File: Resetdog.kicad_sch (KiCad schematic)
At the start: 19 parts, among them U14 MC14541BD, U15 MC74HC4538ADG, U20 74LVC1G17

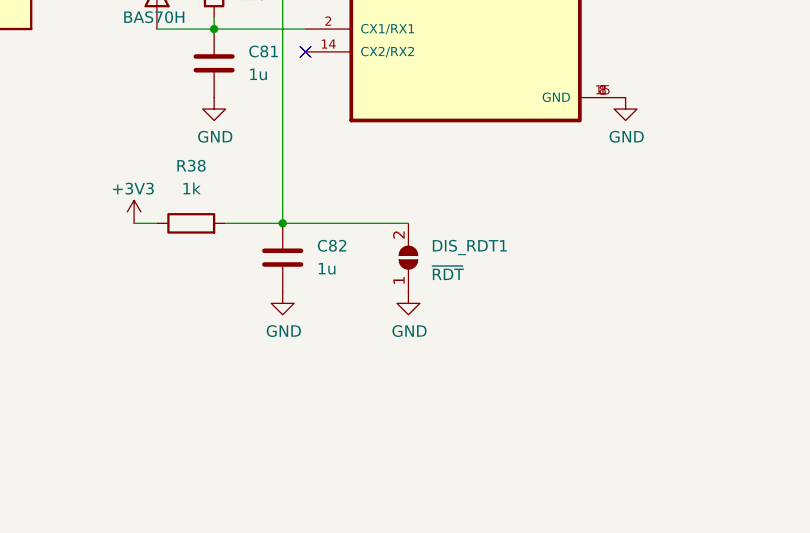
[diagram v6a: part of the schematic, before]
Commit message: Remove disable RTD jumper
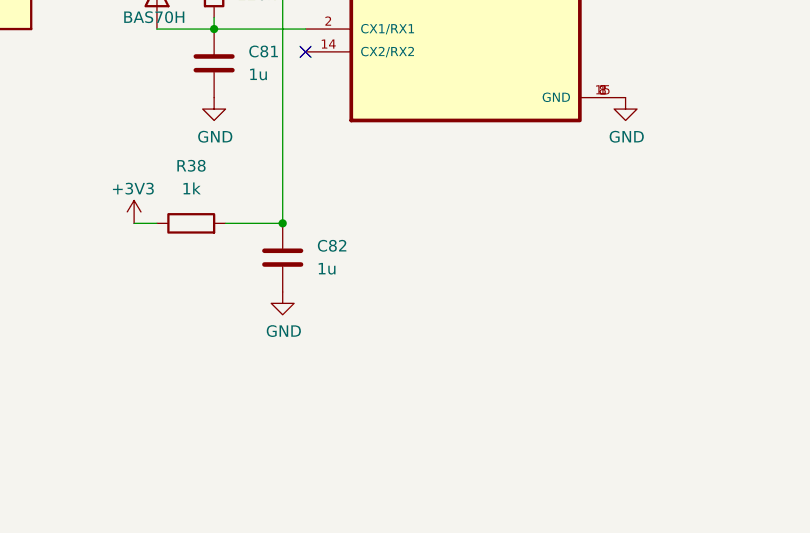
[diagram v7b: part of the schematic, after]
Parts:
- removed DIS_RDT1: ~{RDT}, Jumper:SolderJumper-2_P1.3mm_Open_Pad1.0x1.5mm, symbol Jumper:SolderJumper_2_Open
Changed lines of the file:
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@@
-    (stroke (width 0) (type default) (color 0 0 0 0))
-  )
-  (wire (pts (xy 134.62 119.38) (xy 148.59 119.38))
     (stroke (width 0) (type default) (color 0 0 0 0))
   )
@@
     (pin "2")
   )
-  (symbol (lib_id "power:GND") (at 148.59 127 0) (unit 1)
-    (in_bom yes) (on_board yes)
-    (property "Reference" "#PWR077" (id 0) (at 148.59 133.35 0)
-      (effects (font (size 1.27 1.27)) hide)
-    )
-    (property "Value" "GND" (id 1) (at 148.717 131.3942 0))
-    (property "Footprint" "" (id 2) (at 148.59 127 0)
-      (effects (font (size 1.27 1.27)) hide)
-    )
-    (property "Datasheet" "" (id 3) (at 148.59 127 0)
-      (effects (font (size 1.27 1.27)) hide)
-    )
-    (pin "1")
-  )
   (symbol (lib_id "Device:D") (at 120.65 93.98 270) (unit 1)
     (in_bom yes) (on_board yes)
@@
     (pin "1")
   )
-  (symbol (lib_id "Jumper:SolderJumper_2_Open") (at 148.59 123.19 90) (unit 1)
-    (in_bom no) (on_board yes) (fields_autoplaced)
-    (property "Reference" "DIS_RDT1" (id 0) (at 151.13 121.9199 90)
-      (effects (font (size 1.27 1.27)) (justify right))
-    )
-    (property "Value" "~{RDT}" (id 1) (at 151.13 125.0949 90)
-      (effects (font (size 1.27 1.27)) (justify right))
-    )
-    (property "Footprint" "Jumper:SolderJumper-2_P1.3mm_Open_Pad1.0x1.5mm" (id 2) (at 148.59 123.19 0)
-      (effects (font (size 1.27 1.27)) hide)
-    )
-    (property "Datasheet" "~" (id 3) (at 148.59 123.19 0)
-      (effects (font (size 1.27 1.27)) hide)
-    )
-    (pin "1")
-    (pin "2")
-  )
   (symbol (lib_id "power:+3V3") (at 40.64 127 0) (mirror y) (unit 1)

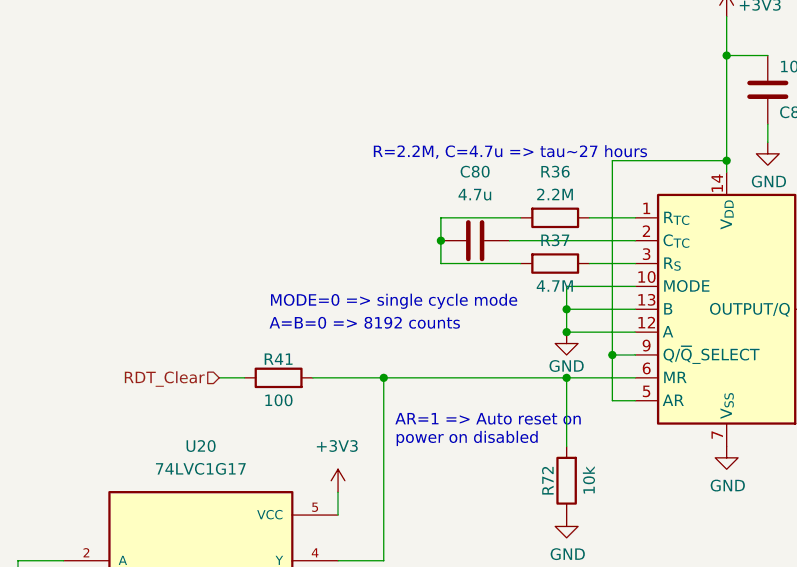
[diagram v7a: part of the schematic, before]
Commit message: Switch RTD MC14541BD IC from single cycle mode to recycle mode, but leave an option to switch back
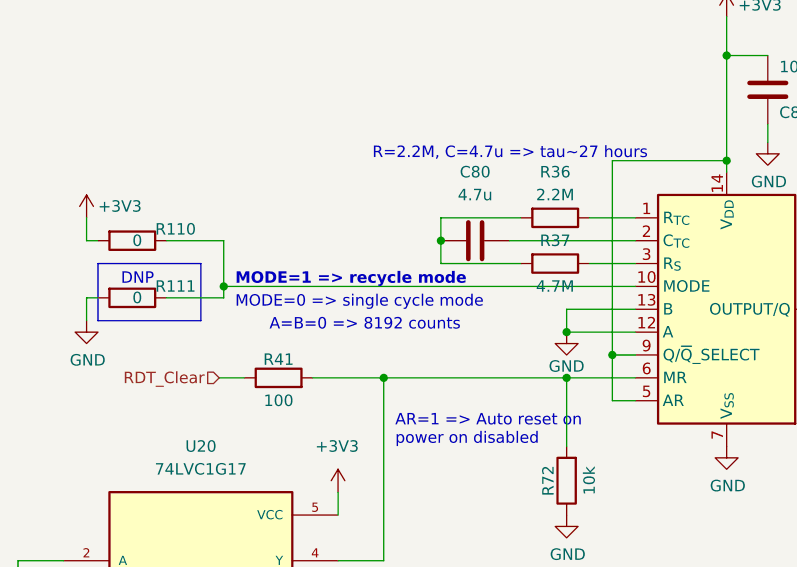
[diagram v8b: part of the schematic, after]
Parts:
- added R110, R111: 0, Resistor_SMD:R_0603_1608Metric, symbol Device:R
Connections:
- net +3V3: now also R110.2
- net GND: now also R111.2; no longer U14.10 (MODE)
- new net: R110.1, R111.1, U14.10 (MODE)
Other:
- note added: "DNP"
- note added: "MODE=1 => recycle mode"
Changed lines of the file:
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@@
   (junction (at 99.06 68.58) (diameter 0) (color 0 0 0 0)
   )
-  (junction (at 81.28 85.09) (diameter 0) (color 0 0 0 0)
-  )
   (junction (at 40.64 137.16) (diameter 0) (color 0 0 0 0)
   )
   (junction (at 99.06 56.896) (diameter 0) (color 0 0 0 0)
+  )
+  (junction (at 43.18 82.55) (diameter 0) (color 0 0 0 0)
   )
   (junction (at 67.31 77.47) (diameter 0) (color 0 0 0 0)
@@
     (stroke (width 0) (type default) (color 0 0 0 0))
   )
+  (polyline (pts (xy 29.21 80.01) (xy 29.21 86.36))
+    (stroke (width 0) (type default) (color 0 0 0 0))
+  )
+  (wire (pts (xy 43.18 77.47) (xy 43.18 82.55))
+    (stroke (width 0) (type default) (color 0 0 0 0))
+  )
   (wire (pts (xy 81.28 92.71) (xy 81.28 100.33))
     (stroke (width 0) (type default) (color 0 0 0 0))
   )
+  (wire (pts (xy 27.94 77.47) (xy 27.94 74.93))
+    (stroke (width 0) (type default) (color 0 0 0 0))
+  )
   (wire (pts (xy 180.34 85.09) (xy 180.34 67.31))
     (stroke (width 0) (type default) (color 0 0 0 0))
@@
     (stroke (width 0) (type default) (color 0 0 0 0))
   )
+  (polyline (pts (xy 29.21 86.36) (xy 40.64 86.36))
+    (stroke (width 0) (type default) (color 0 0 0 0))
+  )
   (wire (pts (xy 88.9 85.09) (xy 81.28 85.09))
     (stroke (width 0) (type default) (color 0 0 0 0))
@@
     (stroke (width 0) (type default) (color 0 0 0 0))
   )
+  (wire (pts (xy 43.18 82.55) (xy 88.9 82.55))
+    (stroke (width 0) (type default) (color 0 0 0 0))
+  )
+  (polyline (pts (xy 29.21 80.01) (xy 40.64 80.01))
+    (stroke (width 0) (type default) (color 0 0 0 0))
+  )
   (wire (pts (xy 83.82 74.93) (xy 88.9 74.93))
     (stroke (width 0) (type default) (color 0 0 0 0))
@@
     (stroke (width 0) (type default) (color 0 0 0 0))
   )
+  (polyline (pts (xy 40.64 86.36) (xy 40.64 80.01))
+    (stroke (width 0) (type default) (color 0 0 0 0))
+  )
   (wire (pts (xy 81.28 87.63) (xy 88.9 87.63))
     (stroke (width 0) (type default) (color 0 0 0 0))
   )
+  (wire (pts (xy 29.21 83.82) (xy 27.94 83.82))
+    (stroke (width 0) (type default) (color 0 0 0 0))
+  )
   (wire (pts (xy 134.62 90.17) (xy 137.16 90.17))
     (stroke (width 0) (type default) (color 0 0 0 0))
@@
     (stroke (width 0) (type default) (color 0 0 0 0))
   )
-  (wire (pts (xy 81.28 82.55) (xy 81.28 85.09))
+  (wire (pts (xy 27.94 83.82) (xy 27.94 86.36))
     (stroke (width 0) (type default) (color 0 0 0 0))
   )
@@
     (stroke (width 0) (type default) (color 0 0 0 0))
   )
-  (wire (pts (xy 88.9 82.55) (xy 81.28 82.55))
-    (stroke (width 0) (type default) (color 0 0 0 0))
-  )
   (wire (pts (xy 118.11 119.38) (xy 120.65 119.38))
     (stroke (width 0) (type default) (color 0 0 0 0))
@@
     (stroke (width 0) (type default) (color 0 0 0 0))
   )
+  (wire (pts (xy 36.83 83.82) (xy 43.18 83.82))
+    (stroke (width 0) (type default) (color 0 0 0 0))
+  )
+  (wire (pts (xy 43.18 83.82) (xy 43.18 82.55))
+    (stroke (width 0) (type default) (color 0 0 0 0))
+  )
   (wire (pts (xy 40.64 137.16) (xy 31.75 137.16))
     (stroke (width 0) (type default) (color 0 0 0 0))
@@
     (stroke (width 0) (type default) (color 0 0 0 0))
   )
+  (wire (pts (xy 29.21 77.47) (xy 27.94 77.47))
+    (stroke (width 0) (type default) (color 0 0 0 0))
+  )
   (wire (pts (xy 81.28 85.09) (xy 81.28 87.63))
     (stroke (width 0) (type default) (color 0 0 0 0))
@@
   )
   (wire (pts (xy 109.22 85.09) (xy 137.16 85.09))
+    (stroke (width 0) (type default) (color 0 0 0 0))
+  )
+  (wire (pts (xy 36.83 77.47) (xy 43.18 77.47))
     (stroke (width 0) (type default) (color 0 0 0 0))
   )
@@
     (effects (font (size 1.778 1.5113)) (justify left bottom))
   )
-  (text "MODE=0 => single cycle mode" (at 48.26 85.09 0)
+  (text "MODE=0 => single cycle mode" (at 44.45 85.09 0)
+    (effects (font (size 1.27 1.27)) (justify left bottom))
+  )
+  (text "DNP" (at 31.75 82.55 0)
     (effects (font (size 1.27 1.27)) (justify left bottom))
   )
@@
     (effects (font (size 1.27 1.27)) (justify left bottom))
   )
+  (text "MODE=1 => recycle mode" (at 44.45 82.55 0)
+    (effects (font (size 1.27 1.27) (thickness 0.254) bold) (justify left bottom))
+  )
   (hierarchical_label "RDT_Clear" (shape input) (at 42.672 92.71 180)
     (effects (font (size 1.27 1.27)) (justify right))
@@
   (hierarchical_label "DCDC_~{Enable}" (shape output) (at 187.96 85.09 0)
     (effects (font (size 1.27 1.27)) (justify left))
+  )
+  (symbol (lib_id "power:+3V3") (at 27.94 74.93 0) (unit 1)
+    (in_bom yes) (on_board yes)
+    (property "Reference" "#PWR085" (id 0) (at 27.94 78.74 0)
+      (effects (font (size 1.27 1.27)) hide)
+    )
+    (property "Value" "+3V3" (id 1) (at 29.21 73.66 0)
+      (effects (font (size 1.27 1.27)) (justify left))
+    )
+    (property "Footprint" "" (id 2) (at 27.94 74.93 0)
+      (effects (font (size 1.27 1.27)) hide)
+    )
+    (property "Datasheet" "" (id 3) (at 27.94 74.93 0)
+      (effects (font (size 1.27 1.27)) hide)
+    )
+    (pin "1")
+  )
+  (symbol (lib_id "Device:R") (at 33.02 77.47 270) (unit 1)
+    (in_bom yes) (on_board yes)
+    (property "Reference" "R110" (id 0) (at 35.56 76.2 90)
+      (effects (font (size 1.27 1.27)) (justify left))
+    )
+    (property "Value" "0" (id 1) (at 33.02 77.47 90)
+      (effects (font (size 1.27 1.27)) (justify left))
+    )
+    (property "Footprint" "Resistor_SMD:R_0603_1608Metric" (id 2) (at 33.02 75.692 90)
+      (effects (font (size 1.27 1.27)) hide)
+    )
+    (property "Datasheet" "~" (id 3) (at 33.02 77.47 0)
+      (effects (font (size 1.27 1.27)) hide)
+    )
+    (property "JLCPCB Part #" "C4117710" (id 4) (at 33.02 77.47 0)
+      (effects (font (size 1.27 1.27)) hide)
+    )
+    (property "Manufacturer_Part_Number" "ERJ-H3G0R00V" (id 5) (at 33.02 77.47 0)
+      (effects (font (size 1.27 1.27)) hide)
+    )
+    (pin "1")
+    (pin "2")
   )
   (symbol (lib_id "Device:R") (at 127 92.71 0) (unit 1)
@@
     )
     (property "Manufacturer_Part_Number" "ERJ-H3EF1002V" (id 5) (at 81.28 104.14 0)
+      (effects (font (size 1.27 1.27)) hide)
+    )
+    (pin "1")
+    (pin "2")
+  )
+  (symbol (lib_id "Device:R") (at 33.02 83.82 270) (unit 1)
+    (in_bom no) (on_board yes)
+    (property "Reference" "R111" (id 0) (at 35.56 82.55 90)
+      (effects (font (size 1.27 1.27)) (justify left))
+    )
+    (property "Value" "0" (id 1) (at 33.02 83.82 90)
+      (effects (font (size 1.27 1.27)) (justify left))
+    )
+    (property "Footprint" "Resistor_SMD:R_0603_1608Metric" (id 2) (at 33.02 82.042 90)
+      (effects (font (size 1.27 1.27)) hide)
+    )
+    (property "Datasheet" "~" (id 3) (at 33.02 83.82 0)
+      (effects (font (size 1.27 1.27)) hide)
+    )
+    (property "JLCPCB Part #" "C4117710" (id 4) (at 33.02 83.82 0)
+      (effects (font (size 1.27 1.27)) hide)
+    )
+    (property "Manufacturer_Part_Number" "ERJ-H3G0R00V" (id 5) (at 33.02 83.82 0)
       (effects (font (size 1.27 1.27)) hide)
     )
@@
     (pin "2")
   )
+  (symbol (lib_id "power:GND") (at 27.94 86.36 0) (unit 1)
+    (in_bom yes) (on_board yes)
+    (property "Reference" "#PWR086" (id 0) (at 27.94 92.71 0)
+      (effects (font (size 1.27 1.27)) hide)
+    )
+    (property "Value" "GND" (id 1) (at 28.067 90.7542 0))
+    (property "Footprint" "" (id 2) (at 27.94 86.36 0)
+      (effects (font (size 1.27 1.27)) hide)
+    )
+    (property "Datasheet" "" (id 3) (at 27.94 86.36 0)
+      (effects (font (size 1.27 1.27)) hide)
+    )
+    (pin "1")
+  )
   (symbol (lib_id "Device:D") (at 27.94 137.16 0) (mirror x) (unit 1)
